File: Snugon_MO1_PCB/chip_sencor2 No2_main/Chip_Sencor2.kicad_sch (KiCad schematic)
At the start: 37 parts, among them J1 Conn_01x8_Pin + 2, J3 USB_C_Receptacle_USB2.0, J6 Conn_01x8_Pin + 2, SW10 RESET, SW9 BOOT, SW9 SW_PUSH, U1 NCP1117-3.3_SOT223, U1 RP2040, U3 W25Q128JVSIQ, Y1 12MHz

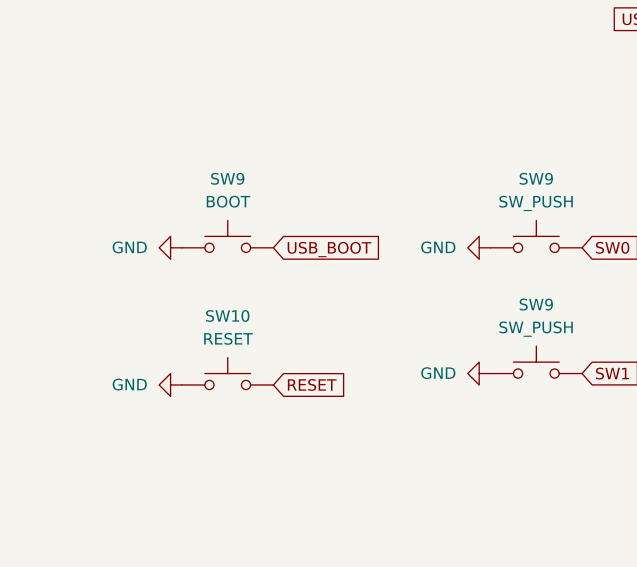
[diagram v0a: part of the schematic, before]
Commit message: リセットボタンとブートボタンの配線修正
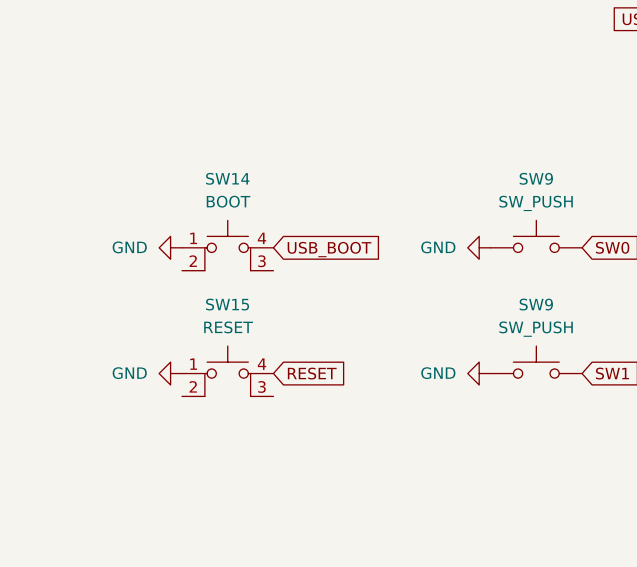
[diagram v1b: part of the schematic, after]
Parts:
- removed SW10: RESET, 0:SW-SMD_4P-L5.1-W5.1-P3.70-LS6.5-TL-2, symbol Switch:SW_Push
- removed SW9: BOOT, 0:SW-SMD_4P-L5.1-W5.1-P3.70-LS6.5-TL-2, symbol Switch:SW_Push
- added SW14: BOOT, 0:SW-SMD_4P-L5.1-W5.1-P3.70-LS6.5-TL-2, symbol Switch:SW_MEC_5E
- added SW15: RESET, 0:SW-SMD_4P-L5.1-W5.1-P3.70-LS6.5-TL-2, symbol Switch:SW_MEC_5E
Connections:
- net GND: now also SW14.1, SW15.1
- net RESET: now also SW15.4 (A)
- net USB_BOOT: now also SW14.4 (A)
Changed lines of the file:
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@@
-    )
-  )
-  (global_label "RESET" (shape input) (at 43.18 127 0) (fields_autoplaced)
-    (effects (font (size 1.27 1.27)) (justify left))
-    (property "Intersheetrefs" "${INTERSHEET_REFS}" (at 51.3383 126.9206 0)
-      (effects (font (size 1.27 1.27)) (justify left) hide)
     )
   )
@@
     )
   )
+  (global_label "RESET" (shape input) (at 43.18 125.73 0) (fields_autoplaced)
+    (effects (font (size 1.27 1.27)) (justify left))
+    (property "Intersheetrefs" "${INTERSHEET_REFS}" (at 51.3383 125.6506 0)
+      (effects (font (size 1.27 1.27)) (justify left) hide)
+    )
+  )
   (global_label "D-" (shape input) (at 212.09 80.01 180) (fields_autoplaced)
     (effects (font (size 1.27 1.27)) (justify right))
@@
     )
   )
-  (symbol (lib_id "power:GND") (at 33.02 127 270) (unit 1)
-    (in_bom yes) (on_board yes) (dnp no) (fields_autoplaced)
-    (property "Reference" "#PWR050" (at 26.67 127 0)
-      (effects (font (size 1.27 1.27)) hide)
-    )
-    (property "Value" "GND" (at 29.21 127 90)
-      (effects (font (size 1.27 1.27)) (justify right))
-    )
-    (property "Footprint" "" (at 33.02 127 0)
-      (effects (font (size 1.27 1.27)) hide)
-    )
-    (property "Datasheet" "" (at 33.02 127 0)
-      (effects (font (size 1.27 1.27)) hide)
-    )
-    (pin "1")
-    (instances
-      (project "RP2040_8key"
-        (path "/67ac9778-0804-43fe-9cd6-2adc6497d786"
-          (reference "#PWR050") (unit 1)
-        )
-      )
-      (project "Chip_Sencor2"
-        (path "/f629c59c-51ca-4d79-b5f3-c4e334ca493d"
-          (reference "#PWR065") (unit 1)
-        )
-      )
-    )
-  )
   (symbol (lib_id "power:+3V3") (at 151.13 27.94 270) (unit 1)
     (in_bom yes) (on_board yes) (dnp no)
@@
     )
   )
-  (symbol (lib_id "Switch:SW_Push") (at 38.1 127 0) (unit 1)
-    (in_bom yes) (on_board yes) (dnp no)
-    (property "Reference" "SW10" (at 38.1 119.38 0)
-      (effects (font (size 1.27 1.27)))
-    )
-    (property "Value" "RESET" (at 38.1 121.92 0)
-      (effects (font (size 1.27 1.27)))
-    )
-    (property "Footprint" "0:SW-SMD_4P-L5.1-W5.1-P3.70-LS6.5-TL-2" (at 38.1 121.92 0)
-      (effects (font (size 1.27 1.27)) hide)
-    )
-    (property "Datasheet" "~" (at 38.1 121.92 0)
-      (effects (font (size 1.27 1.27)) hide)
-    )
-    (property "LCSC" "C318884" (at 38.1 127 0)
-      (effects (font (size 1.27 1.27)) hide)
-    )
-    (property "フィールド4" "Basic" (at 38.1 127 0)
-      (effects (font (size 1.27 1.27)) hide)
-    )
-    (pin "1")
-    (pin "2")
-    (instances
-      (project "RP2040_8key"
-        (path "/67ac9778-0804-43fe-9cd6-2adc6497d786"
-          (reference "SW10") (unit 1)
-        )
-      )
-      (project "Chip_Sencor2"
-        (path "/f629c59c-51ca-4d79-b5f3-c4e334ca493d"
-          (reference "SW13") (unit 1)
-        )
-      )
-    )
-  )
   (symbol (lib_id "power:GND") (at 255.27 29.21 0) (unit 1)
     (in_bom yes) (on_board yes) (dnp no) (fields_autoplaced)
@@
     )
   )
+  (symbol (lib_id "power:GND") (at 33.02 125.73 270) (unit 1)
+    (in_bom yes) (on_board yes) (dnp no) (fields_autoplaced)
+    (property "Reference" "#PWR047" (at 26.67 125.73 0)
+      (effects (font (size 1.27 1.27)) hide)
+    )
+    (property "Value" "GND" (at 29.21 125.73 90)
+      (effects (font (size 1.27 1.27)) (justify right))
+    )
+    (property "Footprint" "" (at 33.02 125.73 0)
+      (effects (font (size 1.27 1.27)) hide)
+    )
+    (property "Datasheet" "" (at 33.02 125.73 0)
+      (effects (font (size 1.27 1.27)) hide)
+    )
+    (pin "1")
+    (instances
+      (project "RP2040_8key"
+        (path "/67ac9778-0804-43fe-9cd6-2adc6497d786"
+          (reference "#PWR047") (unit 1)
+        )
+      )
+      (project "Chip_Sencor2"
+        (path "/f629c59c-51ca-4d79-b5f3-c4e334ca493d"
+          (reference "#PWR08") (unit 1)
+        )
+      )
+    )
+  )
   (symbol (lib_id "Device:R_Small") (at 95.25 86.36 90) (unit 1)
     (in_bom yes) (on_board yes) (dnp no)
@@
     )
   )
+  (symbol (lib_id "Switch:SW_MEC_5E") (at 38.1 128.27 0) (unit 1)
+    (in_bom yes) (on_board yes) (dnp no) (fields_autoplaced)
+    (property "Reference" "SW15" (at 38.1 118.11 0)
+      (effects (font (size 1.27 1.27)))
+    )
+    (property "Value" "RESET" (at 38.1 120.65 0)
+      (effects (font (size 1.27 1.27)))
+    )
+    (property "Footprint" "0:SW-SMD_4P-L5.1-W5.1-P3.70-LS6.5-TL-2" (at 38.1 120.65 0)
+      (effects (font (size 1.27 1.27)) hide)
+    )
+    (property "Datasheet" "http://www.apem.com/int/index.php?controller=attachment&id_attachment=1371" (at 38.1 120.65 0)
+      (effects (font (size 1.27 1.27)) hide)
+    )
+    (property "LCSC" "C318884" (at 38.1 128.27 0)
+      (effects (font (size 1.27 1.27)) hide)
+    )
+    (pin "1")
+    (pin "2")
+    (pin "3")
+    (pin "4")
+    (instances
+      (project "Chip_Sencor2"
+        (path "/f629c59c-51ca-4d79-b5f3-c4e334ca493d"
+          (reference "SW15") (unit 1)
+        )
+      )
+    )
+  )
   (symbol (lib_id "power:GND") (at 83.82 181.61 90) (mirror x) (unit 1)
     (in_bom yes) (on_board yes) (dnp no)
@@
         (path "/f629c59c-51ca-4d79-b5f3-c4e334ca493d"
           (reference "#PWR034") (unit 1)
+        )
+      )
+    )
+  )
+  (symbol (lib_id "Switch:SW_MEC_5E") (at 38.1 114.3 0) (unit 1)
+    (in_bom yes) (on_board yes) (dnp no) (fields_autoplaced)
+    (property "Reference" "SW14" (at 38.1 104.14 0)
+      (effects (font (size 1.27 1.27)))
+    )
+    (property "Value" "BOOT" (at 38.1 106.68 0)
+      (effects (font (size 1.27 1.27)))
+    )
+    (property "Footprint" "0:SW-SMD_4P-L5.1-W5.1-P3.70-LS6.5-TL-2" (at 38.1 106.68 0)
+      (effects (font (size 1.27 1.27)) hide)
+    )
+    (property "Datasheet" "http://www.apem.com/int/index.php?controller=attachment&id_attachment=1371" (at 38.1 106.68 0)
+      (effects (font (size 1.27 1.27)) hide)
+    )
+    (property "LCSC" "C318884" (at 38.1 114.3 0)
+      (effects (font (size 1.27 1.27)) hide)
+    )
+    (pin "1")
+    (pin "2")
+    (pin "3")
+    (pin "4")
+    (instances
+      (project "Chip_Sencor2"
+        (path "/f629c59c-51ca-4d79-b5f3-c4e334ca493d"
+          (reference "SW14") (unit 1)
         )
       )
@@
         )
       )
-    )
-  )
-  (symbol (lib_id "Switch:SW_Push") (at 38.1 111.76 0) (unit 1)
-    (in_bom yes) (on_board yes) (dnp no) (fields_autoplaced)
-    (property "Reference" "SW9" (at 38.1 104.14 0)
-      (effects (font (size 1.27 1.27)))
-    )
-    (property "Value" "BOOT" (at 38.1 106.68 0)
-      (effects (font (size 1.27 1.27)))
-    )
-    (property "Footprint" "0:SW-SMD_4P-L5.1-W5.1-P3.70-LS6.5-TL-2" (at 38.1 106.68 0)
-      (effects (font (size 1.27 1.27)) hide)
-    )
-    (property "Datasheet" "~" (at 38.1 106.68 0)
-      (effects (font (size 1.27 1.27)) hide)
-    )
-    (property "LCSC" "C318884" (at 38.1 111.76 0)
-      (effects (font (size 1.27 1.27)) hide)
-    )
-    (property "フィールド4" "Basic" (at 38.1 111.76 0)
-      (effects (font (size 1.27 1.27)) hide)
-    )
-    (pin "1")
-    (pin "2")
-    (instances
-      (project "RP2040_8key"
-        (path "/67ac9778-0804-43fe-9cd6-2adc6497d786"
-          (reference "SW9") (unit 1)
-        )
-      )
-      (project "Chip_Sencor2"
-        (path "/f629c59c-51ca-4d79-b5f3-c4e334ca493d"
-          (reference "SW12") (unit 1)
-        )
-      )

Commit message: スイッチとエンコーダーはPCBAしない
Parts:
- SW9: LCSC C400268 -> (none)
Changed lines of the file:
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@@
       (effects (font (size 1.27 1.27)) hide)
     )
-    (property "LCSC" "C400268" (at 72.39 111.76 0)
+    (property "LCSC" "" (at 72.39 111.76 0)
       (effects (font (size 1.27 1.27)) hide)
     )
@@
       (effects (font (size 1.27 1.27)) hide)
     )
-    (property "LCSC" "C400268" (at 72.39 125.73 0)
-      (effects (font (size 1.27 1.27)) hide)
-    )
+    (property "LCSC" "" (at 72.39 125.73 0)
+      (effects (font (size 1.27 1.27)) hide)
+    )

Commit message: エンコーダの配線修正
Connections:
- net RE0B: now also U1.35 (GPIO23); no longer U1.2 (GPIO0)
- no-connect marks 9 -> 22
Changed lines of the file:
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@@
   (no_connect (at 44.45 55.88))
   (no_connect (at 44.45 58.42))
+  (no_connect (at 262.89 97.79))
+  (no_connect (at 33.02 114.3))
   (no_connect (at 119.38 176.53))
+  (no_connect (at 262.89 102.87))
+  (no_connect (at 262.89 92.71))
+  (no_connect (at 262.89 69.85))
+  (no_connect (at 262.89 95.25))
   (no_connect (at 119.38 173.99))
+  (no_connect (at 43.18 128.27))
   (no_connect (at 262.89 105.41))
   (no_connect (at 212.09 138.43))
+  (no_connect (at 262.89 125.73))
+  (no_connect (at 262.89 90.17))
+  (no_connect (at 43.18 114.3))
+  (no_connect (at 33.02 128.27))
+  (no_connect (at 262.89 100.33))
   (no_connect (at 212.09 135.89))
+  (no_connect (at 262.89 130.81))
   (no_connect (at 262.89 110.49))
   (wire (pts (xy 29.21 71.12) (xy 31.75 71.12))
@@
     )
   )
+  (global_label "RE0B" (shape input) (at 262.89 128.27 0) (fields_autoplaced)
+    (effects (font (size 1.27 1.27)) (justify left))
+    (property "Intersheetrefs" "${INTERSHEET_REFS}" (at 270.6943 128.27 0)
+      (effects (font (size 1.27 1.27)) (justify left) hide)
+    )
+  )
   (global_label "D-" (shape input) (at 66.04 43.18 0) (fields_autoplaced)
     (effects (font (size 1.27 1.27)) (justify left))
@@
     )
   )
-  (global_label "SW9" (shape input) (at 262.89 204.47 0) (fields_autoplaced)
-    (effects (font (size 1.27 1.27)) (justify left))
-    (property "Intersheetrefs" "${INTERSHEET_REFS}" (at 269.6662 204.47 0)
-      (effects (font (size 1.27 1.27)) (justify left) hide)
-    )
-  )
   (global_label "QSPI_SS" (shape input) (at 101.6 86.36 270) (fields_autoplaced)
     (effects (font (size 1.27 1.27)) (justify right))
@@
     )
   )
-  (global_label "RE0B" (shape input) (at 262.89 69.85 0) (fields_autoplaced)
-    (effects (font (size 1.27 1.27)) (justify left))
-    (property "Intersheetrefs" "${INTERSHEET_REFS}" (at 270.6943 69.85 0)
-      (effects (font (size 1.27 1.27)) (justify left) hide)
-    )
-  )
